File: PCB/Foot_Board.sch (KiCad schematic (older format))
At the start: 8 parts

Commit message: Finished schematic
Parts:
- removed C? (x2): C_Small, symbol Device:C_Small
- removed J? (x2): Conn_01x03, symbol Connector_Generic:Conn_01x03
- removed R? (x2): R_Small_US, symbol Device:R_Small_US
- added C? (x2): 47 uF, symbol Device:C_Small
- added J?: Conn_02x03_Counter_Clockwise, symbol Connector_Generic:Conn_02x03_Counter_Clockwise
- added R? (x2): 10K Ohm, symbol Device:R_Small_US
- C?: value C_Small -> 47 uF
- R?: value R_Small_US -> 10K Ohm
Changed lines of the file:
@@
 $Descr A4 11693 8268
 encoding utf-8
-Sheet 2 4
+Sheet 2 3
 Title ""
 Date ""
@@
 AR Path="/611CB06B/611C4CD5" Ref="C?"  Part="1"
 F 0 "C?" H 6308 2654 50  0000 R CNN
-F 1 "C_Small" H 6308 2745 50  0000 R CNN
+F 1 "47 uF" H 6308 2745 50  0000 R CNN
 F 2 "" H 6400 2700 50  0001 C CNN
 F 3 "~" H 6400 2700 50  0001 C CNN
@@
 AR Path="/611CB06B/611C4CDB" Ref="R?"  Part="1"
 F 0 "R?" H 5818 2746 50  0000 L CNN
-F 1 "R_Small_US" H 5818 2655 50  0000 L CNN
+F 1 "10K Ohm" H 5818 2655 50  0000 L CNN
 F 2 "" H 5750 2700 50  0001 C CNN
 F 3 "~" H 5750 2700 50  0001 C CNN
@@
 Connection ~ 6400 2400
 Connection ~ 5750 2400
-$Comp
-L Connector_Generic:Conn_01x03 J?
-U 1 1 611C5A34
-P 4600 2500
-AR Path="/611C8367/611C5A34" Ref="J?"  Part="1"
-AR Path="/611CB06B/611C5A34" Ref="J?"  Part="1"
-F 0 "J?" H 4550 2800 50  0000 L CNN
-F 1 "Conn_01x03" H 4350 2700 50  0000 L CNN
-F 2 "" H 4600 2500 50  0001 C CNN
-F 3 "~" H 4600 2500 50  0001 C CNN
-	1    4600 2500
-	1    0    0    -1
-$EndComp
-$Comp
-L Connector_Generic:Conn_01x03 J?
-U 1 1 611C66CC
-P 5000 2500
-AR Path="/611C8367/611C66CC" Ref="J?"  Part="1"
-AR Path="/611CB06B/611C66CC" Ref="J?"  Part="1"
-F 0 "J?" H 4918 2817 50  0000 C CNN
-F 1 "Conn_01x03" H 4918 2726 50  0000 C CNN
-F 2 "" H 5000 2500 50  0001 C CNN
-F 3 "~" H 5000 2500 50  0001 C CNN
-	1    5000 2500
-	-1   0    0    -1
-$EndComp
-Text HLabel 3400 2400 0    50   Input ~ 0
+Text HLabel 4200 2500 0    50   Input ~ 0
 Sensor_Power
 Wire Wire Line
-	3650 2400 4400 2400
-Wire Wire Line
-	3650 2500 4400 2500
-Wire Wire Line
-	3650 2600 4400 2600
-Wire Wire Line
-	3650 2400 3650 2500
-Connection ~ 3650 2500
-Wire Wire Line
-	3650 2500 3650 2600
-Wire Wire Line
-	3650 2400 3400 2400
-Connection ~ 3650 2400
-$Comp
-L Device:C_Small C?
-U 1 1 611CFFC0
-P 6400 3700
-AR Path="/611CFFC0" Ref="C?"  Part="1"
-AR Path="/611C8367/611C9C0B/611CFFC0" Ref="C?"  Part="1"
-AR Path="/611C8367/611C96D8/611CFFC0" Ref="C?"  Part="1"
-AR Path="/611C8367/611C9C62/611CFFC0" Ref="C?"  Part="1"
-AR Path="/611CB06B/611C96D8/611CFFC0" Ref="C?"  Part="1"
-AR Path="/611CB06B/611C9C0B/611CFFC0" Ref="C?"  Part="1"
-AR Path="/611CB06B/611C9C62/611CFFC0" Ref="C?"  Part="1"
-AR Path="/611C8367/611CFFC0" Ref="C?"  Part="1"
-AR Path="/611CB06B/611CFFC0" Ref="C?"  Part="1"
-F 0 "C?" H 6308 3654 50  0000 R CNN
-F 1 "C_Small" H 6308 3745 50  0000 R CNN
-F 2 "" H 6400 3700 50  0001 C CNN
-F 3 "~" H 6400 3700 50  0001 C CNN
-	1    6400 3700
-	-1   0    0    1
-$EndComp
-$Comp
-L Device:R_Small_US R?
-U 1 1 611CFFC6
-P 5750 3700
-AR Path="/611CFFC6" Ref="R?"  Part="1"
-AR Path="/611C8367/611C9C0B/611CFFC6" Ref="R?"  Part="1"
-AR Path="/611C8367/611C96D8/611CFFC6" Ref="R?"  Part="1"
-AR Path="/611C8367/611C9C62/611CFFC6" Ref="R?"  Part="1"
-AR Path="/611CB06B/611C96D8/611CFFC6" Ref="R?"  Part="1"
-AR Path="/611CB06B/611C9C0B/611CFFC6" Ref="R?"  Part="1"
-AR Path="/611CB06B/611C9C62/611CFFC6" Ref="R?"  Part="1"
-AR Path="/611C8367/611CFFC6" Ref="R?"  Part="1"
-AR Path="/611CB06B/611CFFC6" Ref="R?"  Part="1"
-F 0 "R?" H 5818 3746 50  0000 L CNN
-F 1 "R_Small_US" H 5818 3655 50  0000 L CNN
-F 2 "" H 5750 3700 50  0001 C CNN
-F 3 "~" H 5750 3700 50  0001 C CNN
-	1    5750 3700
-	1    0    0    -1
-$EndComp
+	4450 2500 4200 2500
 $Comp
 L BPSDisplay:GND #PWR?
@@
 Connection ~ 5750 3400
 $Comp
-L Device:C_Small C?
-U 1 1 611D0D2A
-P 6400 4700
-AR Path="/611D0D2A" Ref="C?"  Part="1"
-AR Path="/611C8367/611C9C0B/611D0D2A" Ref="C?"  Part="1"
-AR Path="/611C8367/611C96D8/611D0D2A" Ref="C?"  Part="1"
-AR Path="/611C8367/611C9C62/611D0D2A" Ref="C?"  Part="1"
-AR Path="/611CB06B/611C96D8/611D0D2A" Ref="C?"  Part="1"
-AR Path="/611CB06B/611C9C0B/611D0D2A" Ref="C?"  Part="1"
-AR Path="/611CB06B/611C9C62/611D0D2A" Ref="C?"  Part="1"
-AR Path="/611C8367/611D0D2A" Ref="C?"  Part="1"
-AR Path="/611CB06B/611D0D2A" Ref="C?"  Part="1"
-F 0 "C?" H 6308 4654 50  0000 R CNN
-F 1 "C_Small" H 6308 4745 50  0000 R CNN
-F 2 "" H 6400 4700 50  0001 C CNN
-F 3 "~" H 6400 4700 50  0001 C CNN
-	1    6400 4700
-	-1   0    0    1
-$EndComp
-$Comp
-L Device:R_Small_US R?
-U 1 1 611D0D30
-P 5750 4700
-AR Path="/611D0D30" Ref="R?"  Part="1"
-AR Path="/611C8367/611C9C0B/611D0D30" Ref="R?"  Part="1"
-AR Path="/611C8367/611C96D8/611D0D30" Ref="R?"  Part="1"
-AR Path="/611C8367/611C9C62/611D0D30" Ref="R?"  Part="1"
-AR Path="/611CB06B/611C96D8/611D0D30" Ref="R?"  Part="1"
-AR Path="/611CB06B/611C9C0B/611D0D30" Ref="R?"  Part="1"
-AR Path="/611CB06B/611C9C62/611D0D30" Ref="R?"  Part="1"
-AR Path="/611C8367/611D0D30" Ref="R?"  Part="1"
-AR Path="/611CB06B/611D0D30" Ref="R?"  Part="1"
-F 0 "R?" H 5818 4746 50  0000 L CNN
-F 1 "R_Small_US" H 5818 4655 50  0000 L CNN
-F 2 "" H 5750 4700 50  0001 C CNN
-F 3 "~" H 5750 4700 50  0001 C CNN
-	1    5750 4700
-	1    0    0    -1
-$EndComp
-$Comp
 L BPSDisplay:GND #PWR?
 U 1 1 611D0D36
@@
 Text HLabel 7900 2300 2    50   Output ~ 0
 Data_Out[1..3]
+$Comp
+L Connector_Generic:Conn_02x03_Counter_Clockwise J?
+U 1 1 611D5C2C
+P 4900 2500
+F 0 "J?" H 4950 2817 50  0000 C CNN
+F 1 "Conn_02x03_Counter_Clockwise" H 4950 2726 50  0000 C CNN
+F 2 "" H 4900 2500 50  0001 C CNN
+F 3 "~" H 4900 2500 50  0001 C CNN
+	1    4900 2500
+	1    0    0    -1
+$EndComp
+$Comp
+L Device:C_Small C?
+U 1 1 611E994E
+P 6400 3700
+AR Path="/611E994E" Ref="C?"  Part="1"
+AR Path="/611C8367/611C9C0B/611E994E" Ref="C?"  Part="1"
+AR Path="/611C8367/611C96D8/611E994E" Ref="C?"  Part="1"
+AR Path="/611C8367/611C9C62/611E994E" Ref="C?"  Part="1"
+AR Path="/611CB06B/611C96D8/611E994E" Ref="C?"  Part="1"
+AR Path="/611CB06B/611C9C0B/611E994E" Ref="C?"  Part="1"
+AR Path="/611CB06B/611C9C62/611E994E" Ref="C?"  Part="1"
+AR Path="/611C8367/611E994E" Ref="C?"  Part="1"
+AR Path="/611CB06B/611E994E" Ref="C?"  Part="1"
+F 0 "C?" H 6308 3654 50  0000 R CNN
+F 1 "47 uF" H 6308 3745 50  0000 R CNN
+F 2 "" H 6400 3700 50  0001 C CNN
+F 3 "~" H 6400 3700 50  0001 C CNN
+	1    6400 3700
+	-1   0    0    1
+$EndComp
+$Comp
+L Device:C_Small C?
+U 1 1 611E9C41
+P 6400 4700
+AR Path="/611E9C41" Ref="C?"  Part="1"
+AR Path="/611C8367/611C9C0B/611E9C41" Ref="C?"  Part="1"
+AR Path="/611C8367/611C96D8/611E9C41" Ref="C?"  Part="1"
+AR Path="/611C8367/611C9C62/611E9C41" Ref="C?"  Part="1"
+AR Path="/611CB06B/611C96D8/611E9C41" Ref="C?"  Part="1"
+AR Path="/611CB06B/611C9C0B/611E9C41" Ref="C?"  Part="1"
+AR Path="/611CB06B/611C9C62/611E9C41" Ref="C?"  Part="1"
+AR Path="/611C8367/611E9C41" Ref="C?"  Part="1"
+AR Path="/611CB06B/611E9C41" Ref="C?"  Part="1"
+F 0 "C?" H 6308 4654 50  0000 R CNN
+F 1 "47 uF" H 6308 4745 50  0000 R CNN
+F 2 "" H 6400 4700 50  0001 C CNN
+F 3 "~" H 6400 4700 50  0001 C CNN
+	1    6400 4700
+	-1   0    0    1
+$EndComp
+Wire Wire Line
+	4700 2400 4450 2400
+Wire Wire Line
+	4450 2400 4450 2500
+Wire Wire Line
+	4700 2500 4450 2500
+Connection ~ 4450 2500
+Wire Wire Line
+	4700 2600 4450 2600
+Wire Wire Line
+	4450 2600 4450 2500
 Wire Bus Line
 	7300 2300 7300 4300
+$Comp
+L Device:R_Small_US R?
+U 1 1 611EC5B5
+P 5750 3700
+AR Path="/611EC5B5" Ref="R?"  Part="1"
+AR Path="/611C8367/611C9C0B/611EC5B5" Ref="R?"  Part="1"
+AR Path="/611C8367/611C96D8/611EC5B5" Ref="R?"  Part="1"
+AR Path="/611C8367/611C9C62/611EC5B5" Ref="R?"  Part="1"
+AR Path="/611CB06B/611C96D8/611EC5B5" Ref="R?"  Part="1"
+AR Path="/611CB06B/611C9C0B/611EC5B5" Ref="R?"  Part="1"
+AR Path="/611CB06B/611C9C62/611EC5B5" Ref="R?"  Part="1"
+AR Path="/611C8367/611EC5B5" Ref="R?"  Part="1"
+AR Path="/611CB06B/611EC5B5" Ref="R?"  Part="1"
+F 0 "R?" H 5818 3746 50  0000 L CNN
+F 1 "10K Ohm" H 5818 3655 50  0000 L CNN
+F 2 "" H 5750 3700 50  0001 C CNN
+F 3 "~" H 5750 3700 50  0001 C CNN
+	1    5750 3700
+	1    0    0    -1
+$EndComp
+$Comp
+L Device:R_Small_US R?
+U 1 1 611ECAE2
+P 5750 4700
+AR Path="/611ECAE2" Ref="R?"  Part="1"
+AR Path="/611C8367/611C9C0B/611ECAE2" Ref="R?"  Part="1"
+AR Path="/611C8367/611C96D8/611ECAE2" Ref="R?"  Part="1"
+AR Path="/611C8367/611C9C62/611ECAE2" Ref="R?"  Part="1"
+AR Path="/611CB06B/611C96D8/611ECAE2" Ref="R?"  Part="1"
+AR Path="/611CB06B/611C9C0B/611ECAE2" Ref="R?"  Part="1"
+AR Path="/611CB06B/611C9C62/611ECAE2" Ref="R?"  Part="1"
+AR Path="/611C8367/611ECAE2" Ref="R?"  Part="1"
+AR Path="/611CB06B/611ECAE2" Ref="R?"  Part="1"
+F 0 "R?" H 5818 4746 50  0000 L CNN
+F 1 "10K Ohm" H 5818 4655 50  0000 L CNN
+F 2 "" H 5750 4700 50  0001 C CNN
+F 3 "~" H 5750 4700 50  0001 C CNN
+	1    5750 4700
+	1    0    0    -1
+$EndComp
 $EndSCHEMATC

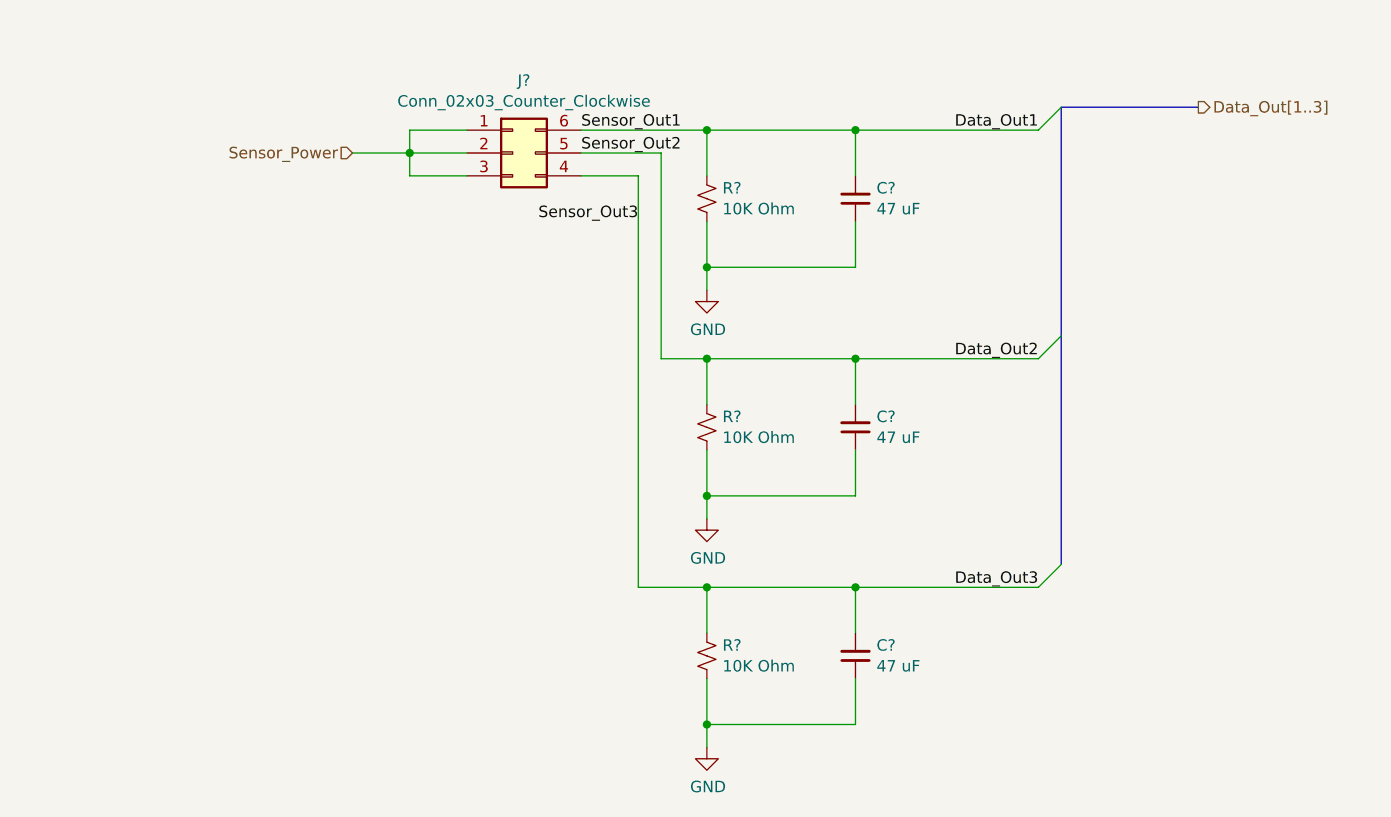
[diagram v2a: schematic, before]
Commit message: Rough layout of pcb
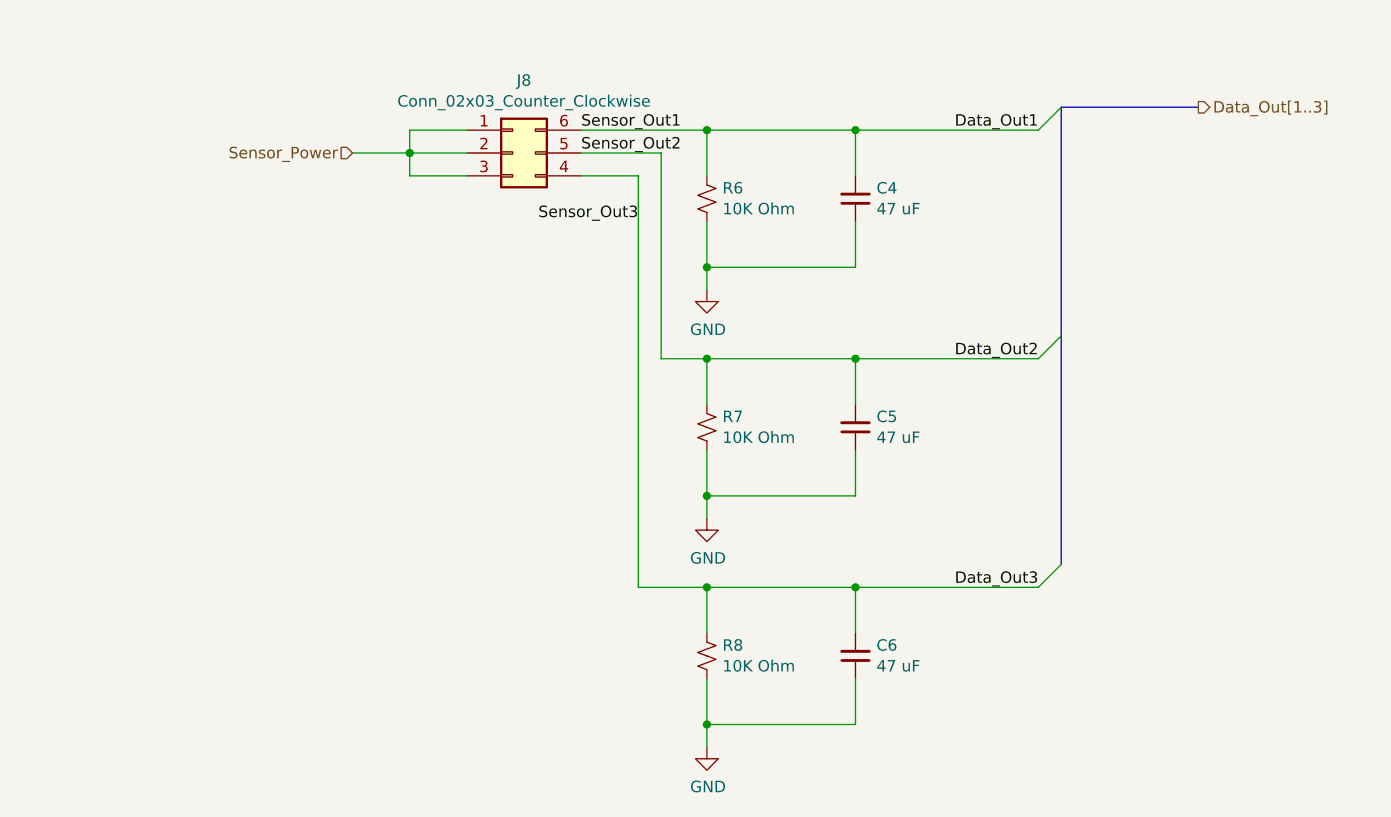
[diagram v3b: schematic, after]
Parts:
- C1, C2, C3: renamed from C?; footprint (none) -> Capacitor_THT:CP_Radial_D5.0mm_P2.50mm
- J7: renamed from J?; footprint (none) -> Connector_Molex:Molex_Micro-Fit_3.0_43045-0600_2x03_P3.00mm_Horizontal
- R3, R4, R5: renamed from R?; footprint (none) -> Resistor_THT:R_Axial_DIN0207_L6.3mm_D2.5mm_P7.62mm_Horizontal
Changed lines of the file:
@@
 $Descr A4 11693 8268
 encoding utf-8
-Sheet 3 3
+Sheet 2 3
 Title ""
 Date ""
@@
 AR Path="/611CB06B/611C9C0B/611C4CD5" Ref="C?"  Part="1"
 AR Path="/611CB06B/611C9C62/611C4CD5" Ref="C?"  Part="1"
-AR Path="/611C8367/611C4CD5" Ref="C?"  Part="1"
-AR Path="/611CB06B/611C4CD5" Ref="C?"  Part="1"
-F 0 "C?" H 6308 2654 50  0000 R CNN
+AR Path="/611C8367/611C4CD5" Ref="C1"  Part="1"
+AR Path="/611CB06B/611C4CD5" Ref="C4"  Part="1"
+F 0 "C4" H 6308 2654 50  0000 R CNN
 F 1 "47 uF" H 6308 2745 50  0000 R CNN
-F 2 "" H 6400 2700 50  0001 C CNN
+F 2 "Capacitor_THT:CP_Radial_D5.0mm_P2.50mm" H 6400 2700 50  0001 C CNN
 F 3 "~" H 6400 2700 50  0001 C CNN
 	1    6400 2700
@@
 AR Path="/611CB06B/611C9C0B/611C4CDB" Ref="R?"  Part="1"
 AR Path="/611CB06B/611C9C62/611C4CDB" Ref="R?"  Part="1"
-AR Path="/611C8367/611C4CDB" Ref="R?"  Part="1"
-AR Path="/611CB06B/611C4CDB" Ref="R?"  Part="1"
-F 0 "R?" H 5818 2746 50  0000 L CNN
+AR Path="/611C8367/611C4CDB" Ref="R3"  Part="1"
+AR Path="/611CB06B/611C4CDB" Ref="R6"  Part="1"
+F 0 "R6" H 5818 2746 50  0000 L CNN
 F 1 "10K Ohm" H 5818 2655 50  0000 L CNN
-F 2 "" H 5750 2700 50  0001 C CNN
+F 2 "Resistor_THT:R_Axial_DIN0207_L6.3mm_D2.5mm_P7.62mm_Horizontal" H 5750 2700 50  0001 C CNN
 F 3 "~" H 5750 2700 50  0001 C CNN
 	1    5750 2700
@@
 AR Path="/611CB06B/611C9C0B/611C4CE1" Ref="#PWR?"  Part="1"
 AR Path="/611CB06B/611C9C62/611C4CE1" Ref="#PWR?"  Part="1"
-AR Path="/611C8367/611C4CE1" Ref="#PWR?"  Part="1"
-AR Path="/611CB06B/611C4CE1" Ref="#PWR?"  Part="1"
-F 0 "#PWR?" H 5750 2850 50  0001 C CNN
+AR Path="/611C8367/611C4CE1" Ref="#PWR010"  Part="1"
+AR Path="/611CB06B/611C4CE1" Ref="#PWR013"  Part="1"
+F 0 "#PWR013" H 5750 2850 50  0001 C CNN
 F 1 "GND" H 5755 2927 50  0000 C CNN
 F 2 "" H 5750 3100 50  0000 C CNN
@@
 AR Path="/611CB06B/611C9C0B/611CFFCC" Ref="#PWR?"  Part="1"
 AR Path="/611CB06B/611C9C62/611CFFCC" Ref="#PWR?"  Part="1"
-AR Path="/611C8367/611CFFCC" Ref="#PWR?"  Part="1"
-AR Path="/611CB06B/611CFFCC" Ref="#PWR?"  Part="1"
-F 0 "#PWR?" H 5750 3850 50  0001 C CNN
+AR Path="/611C8367/611CFFCC" Ref="#PWR011"  Part="1"
+AR Path="/611CB06B/611CFFCC" Ref="#PWR014"  Part="1"
+F 0 "#PWR014" H 5750 3850 50  0001 C CNN
 F 1 "GND" H 5755 3927 50  0000 C CNN
 F 2 "" H 5750 4100 50  0000 C CNN
@@
 AR Path="/611CB06B/611C9C0B/611D0D36" Ref="#PWR?"  Part="1"
 AR Path="/611CB06B/611C9C62/611D0D36" Ref="#PWR?"  Part="1"
-AR Path="/611C8367/611D0D36" Ref="#PWR?"  Part="1"
-AR Path="/611CB06B/611D0D36" Ref="#PWR?"  Part="1"
-F 0 "#PWR?" H 5750 4850 50  0001 C CNN
+AR Path="/611C8367/611D0D36" Ref="#PWR012"  Part="1"
+AR Path="/611CB06B/611D0D36" Ref="#PWR015"  Part="1"
+F 0 "#PWR015" H 5750 4850 50  0001 C CNN
 F 1 "GND" H 5755 4927 50  0000 C CNN
 F 2 "" H 5750 5100 50  0000 C CNN
@@
 Data_Out[1..3]
 $Comp
-L Connector_Generic:Conn_02x03_Counter_Clockwise J?
+L Connector_Generic:Conn_02x03_Counter_Clockwise J7
 U 1 1 611D5C2C
 P 4900 2500
-AR Path="/611C8367/611D5C2C" Ref="J?"  Part="1"
-AR Path="/611CB06B/611D5C2C" Ref="J?"  Part="1"
-F 0 "J?" H 4950 2817 50  0000 C CNN
+AR Path="/611C8367/611D5C2C" Ref="J7"  Part="1"
+AR Path="/611CB06B/611D5C2C" Ref="J8"  Part="1"
+F 0 "J8" H 4950 2817 50  0000 C CNN
 F 1 "Conn_02x03_Counter_Clockwise" H 4950 2726 50  0000 C CNN
-F 2 "" H 4900 2500 50  0001 C CNN
+F 2 "Connector_Molex:Molex_Micro-Fit_3.0_43045-0600_2x03_P3.00mm_Horizontal" H 4900 2500 50  0001 C CNN
 F 3 "~" H 4900 2500 50  0001 C CNN
 	1    4900 2500
@@
 AR Path="/611CB06B/611C9C0B/611E994E" Ref="C?"  Part="1"
 AR Path="/611CB06B/611C9C62/611E994E" Ref="C?"  Part="1"
-AR Path="/611C8367/611E994E" Ref="C?"  Part="1"
-AR Path="/611CB06B/611E994E" Ref="C?"  Part="1"
-F 0 "C?" H 6308 3654 50  0000 R CNN
+AR Path="/611C8367/611E994E" Ref="C2"  Part="1"
+AR Path="/611CB06B/611E994E" Ref="C5"  Part="1"
+F 0 "C5" H 6308 3654 50  0000 R CNN
 F 1 "47 uF" H 6308 3745 50  0000 R CNN
-F 2 "" H 6400 3700 50  0001 C CNN
+F 2 "Capacitor_THT:CP_Radial_D5.0mm_P2.50mm" H 6400 3700 50  0001 C CNN
 F 3 "~" H 6400 3700 50  0001 C CNN
 	1    6400 3700
@@
 AR Path="/611CB06B/611C9C0B/611E9C41" Ref="C?"  Part="1"
 AR Path="/611CB06B/611C9C62/611E9C41" Ref="C?"  Part="1"
-AR Path="/611C8367/611E9C41" Ref="C?"  Part="1"
-AR Path="/611CB06B/611E9C41" Ref="C?"  Part="1"
-F 0 "C?" H 6308 4654 50  0000 R CNN
+AR Path="/611C8367/611E9C41" Ref="C3"  Part="1"
+AR Path="/611CB06B/611E9C41" Ref="C6"  Part="1"
+F 0 "C6" H 6308 4654 50  0000 R CNN
 F 1 "47 uF" H 6308 4745 50  0000 R CNN
-F 2 "" H 6400 4700 50  0001 C CNN
+F 2 "Capacitor_THT:CP_Radial_D5.0mm_P2.50mm" H 6400 4700 50  0001 C CNN
 F 3 "~" H 6400 4700 50  0001 C CNN
 	1    6400 4700
@@
 AR Path="/611CB06B/611C9C0B/611EC5B5" Ref="R?"  Part="1"
 AR Path="/611CB06B/611C9C62/611EC5B5" Ref="R?"  Part="1"
-AR Path="/611C8367/611EC5B5" Ref="R?"  Part="1"
-AR Path="/611CB06B/611EC5B5" Ref="R?"  Part="1"
-F 0 "R?" H 5818 3746 50  0000 L CNN
+AR Path="/611C8367/611EC5B5" Ref="R4"  Part="1"
+AR Path="/611CB06B/611EC5B5" Ref="R7"  Part="1"
+F 0 "R7" H 5818 3746 50  0000 L CNN
 F 1 "10K Ohm" H 5818 3655 50  0000 L CNN
-F 2 "" H 5750 3700 50  0001 C CNN
+F 2 "Resistor_THT:R_Axial_DIN0207_L6.3mm_D2.5mm_P7.62mm_Horizontal" H 5750 3700 50  0001 C CNN
 F 3 "~" H 5750 3700 50  0001 C CNN
 	1    5750 3700
@@
 AR Path="/611CB06B/611C9C0B/611ECAE2" Ref="R?"  Part="1"
 AR Path="/611CB06B/611C9C62/611ECAE2" Ref="R?"  Part="1"
-AR Path="/611C8367/611ECAE2" Ref="R?"  Part="1"
-AR Path="/611CB06B/611ECAE2" Ref="R?"  Part="1"
-F 0 "R?" H 5818 4746 50  0000 L CNN
+AR Path="/611C8367/611ECAE2" Ref="R5"  Part="1"
+AR Path="/611CB06B/611ECAE2" Ref="R8"  Part="1"
+F 0 "R8" H 5818 4746 50  0000 L CNN
 F 1 "10K Ohm" H 5818 4655 50  0000 L CNN
-F 2 "" H 5750 4700 50  0001 C CNN
+F 2 "Resistor_THT:R_Axial_DIN0207_L6.3mm_D2.5mm_P7.62mm_Horizontal" H 5750 4700 50  0001 C CNN
 F 3 "~" H 5750 4700 50  0001 C CNN
 	1    5750 4700
